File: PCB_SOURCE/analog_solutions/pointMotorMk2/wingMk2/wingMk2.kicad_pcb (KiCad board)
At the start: 2 copper layers, 46 x 23.3 mm, 0 parts

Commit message: added missing files. working on ossd mk2 code
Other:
- board size 46 x 23.3 mm -> 46 x 23.5 mm
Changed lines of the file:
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@@
 	)
 	(gr_arc
-		(start -18 -10.8)
-		(mid -17.707107 -11.507107)
-		(end -17 -11.8)
+		(start -18 -11)
+		(mid -17.707107 -11.707107)
+		(end -17 -12)
 		(stroke
 			(width 0.05)
@@
 	)
 	(gr_arc
-		(start -5 -9)
-		(mid -3.585786 -8.414214)
-		(end -3 -7)
+		(start 1.5 1.5)
+		(mid 0 3)
+		(end -1.5 1.5)
+		(stroke
+			(width 0.05)
+			(type default)
+		)
+		(layer "Edge.Cuts")
+	)
+	(gr_arc
+		(start -5.499999 -9)
+		(mid -4.085785 -8.414214)
+		(end -3.499999 -7)
 		(stroke
 			(width 0.05)
@@
 	)
 	(gr_line
-		(start 9 -7)
-		(end 9 1)
-		(stroke
-			(width 0.05)
-			(type default)
-		)
-		(layer "Edge.Cuts")
-	)
-	(gr_arc
-		(start 7 -9)
-		(mid 8.414214 -8.414214)
-		(end 9 -7)
-		(stroke
-			(width 0.05)
-			(type default)
-		)
-		(layer "Edge.Cuts")
-	)
-	(gr_line
-		(start -9 -7)
-		(end -9 1)
+		(start 9.500001 -7)
+		(end 9.500001 1)
+		(stroke
+			(width 0.05)
+			(type default)
+		)
+		(layer "Edge.Cuts")
+	)
+	(gr_arc
+		(start 7.500001 -9)
+		(mid 8.914215 -8.414214)
+		(end 9.500001 -7)
+		(stroke
+			(width 0.05)
+			(type default)
+		)
+		(layer "Edge.Cuts")
+	)
+	(gr_line
+		(start -9.499999 -7)
+		(end -9.499999 1)
 		(stroke
 			(width 0.05)
@@
 	)
 	(gr_arc
-		(start -9 -7)
-		(mid -8.414214 -8.414214)
-		(end -7 -9)
-		(stroke
-			(width 0.05)
-			(type default)
-		)
-		(layer "Edge.Cuts")
-	)
-	(gr_arc
-		(start 5.000001 2.999999)
-		(mid 3.585787 2.414213)
-		(end 3.000001 0.999999)
+		(start -9.499999 -7)
+		(mid -8.914213 -8.414214)
+		(end -7.499999 -9)
+		(stroke
+			(width 0.05)
+			(type default)
+		)
+		(layer "Edge.Cuts")
+	)
+	(gr_arc
+		(start 5.500002 2.999999)
+		(mid 4.085788 2.414213)
+		(end 3.500002 0.999999)
 		(stroke
 			(width 0.05)
@@
 	)
 	(gr_arc
-		(start 8.999999 0.999999)
-		(mid 8.414213 2.414213)
-		(end 6.999999 2.999999)
-		(stroke
-			(width 0.05)
-			(type default)
-		)
-		(layer "Edge.Cuts")
-	)
-	(gr_arc
-		(start -6.999999 2.999999)
-		(mid -8.414213 2.414213)
-		(end -8.999999 0.999999)
+		(start 9.5 0.999999)
+		(mid 8.914214 2.414213)
+		(end 7.5 2.999999)
+		(stroke
+			(width 0.05)
+			(type default)
+		)
+		(layer "Edge.Cuts")
+	)
+	(gr_arc
+		(start -7.499998 2.999999)
+		(mid -8.914212 2.414213)
+		(end -9.499998 0.999999)
 		(stroke
 			(width 0.05)
@@
 	)
 	(gr_line
-		(start 5.000001 2.999999)
-		(end 6.999999 2.999999)
+		(start 5.500002 2.999999)
+		(end 7.5 2.999999)
+		(stroke
+			(width 0.05)
+			(type default)
+		)
+		(layer "Edge.Cuts")
+	)
+	(gr_arc
+		(start -1.5 -7.5)
+		(mid 0 -9)
+		(end 1.5 -7.5)
 		(stroke
 			(width 0.05)
@@
 	)
 	(gr_line
-		(start -1 -7)
-		(end -1 1)
+		(start -1.5 -7.5)
+		(end -1.5 1.5)
 		(stroke
 			(width 0.05)
@@
 	)
 	(gr_line
-		(start -3 -7)
-		(end -3 1)
-		(stroke
-			(width 0.05)
-			(type default)
-		)
-		(layer "Edge.Cuts")
-	)
-	(gr_line
-		(start 28 -6.75)
+		(start -3.499999 -7)
+		(end -3.499999 1)
+		(stroke
+			(width 0.05)
+			(type default)
+		)
+		(layer "Edge.Cuts")
+	)
+	(gr_line
+		(start 28 -6.95)
 		(end 28 3.5)
 		(stroke
@@
 		(layer "Edge.Cuts")
 	)
-	(gr_arc
-		(start 1 1)
-		(mid 0 2)
-		(end -1 1)
-		(stroke
-			(width 0.05)
-			(type default)
-		)
-		(layer "Edge.Cuts")
-	)
-	(gr_line
-		(start 5 -9)
-		(end 7 -9)
-		(stroke
-			(width 0.05)
-			(type default)
-		)
-		(layer "Edge.Cuts")
-	)
-	(gr_arc
-		(start -1 -7)
-		(mid 0 -8)
-		(end 1 -7)
-		(stroke
-			(width 0.05)
-			(type default)
-		)
-		(layer "Edge.Cuts")
-	)
-	(gr_arc
-		(start -3.000001 0.999999)
-		(mid -3.585787 2.414213)
-		(end -5.000001 2.999999)
+	(gr_line
+		(start 5.500001 -9)
+		(end 7.500001 -9)
+		(stroke
+			(width 0.05)
+			(type default)
+		)
+		(layer "Edge.Cuts")
+	)
+	(gr_arc
+		(start -3.5 0.999999)
+		(mid -4.085786 2.414213)
+		(end -5.5 2.999999)
 		(stroke
 			(width 0.05)
@@
 	)
 	(gr_line
-		(start 3 -7)
-		(end 3 1)
-		(stroke
-			(width 0.05)
-			(type default)
-		)
-		(layer "Edge.Cuts")
-	)
-	(gr_line
-		(start 4 -13.3)
-		(end 4 -11.8)
+		(start 3.500001 -7)
+		(end 3.500001 1)
+		(stroke
+			(width 0.05)
+			(type default)
+		)
+		(layer "Edge.Cuts")
+	)
+	(gr_line
+		(start 4 -13.5)
+		(end 4 -12)
 		(stroke
 			(width 0.05)
@@
 	)
 	(gr_line
-		(start -17 -11.8)
-		(end -4 -11.8)
-		(stroke
-			(width 0.05)
-			(type default)
-		)
-		(layer "Edge.Cuts")
-	)
-	(gr_line
-		(start -4 -13.3)
-		(end 4 -13.3)
-		(stroke
-			(width 0.05)
-			(type default)
-		)
-		(layer "Edge.Cuts")
-	)
-	(gr_line
-		(start -7 -9)
-		(end -5 -9)
-		(stroke
-			(width 0.05)
-			(type default)
-		)
-		(layer "Edge.Cuts")
-	)
-	(gr_arc
-		(start 3 -7)
-		(mid 3.585786 -8.414214)
-		(end 5 -9)
-		(stroke
-			(width 0.05)
-			(type default)
-		)
-		(layer "Edge.Cuts")
-	)
-	(gr_line
-		(start 4 -11.8)
-		(end 23 -11.8)
+		(start -17 -12)
+		(end -4 -12)
+		(stroke
+			(width 0.05)
+			(type default)
+		)
+		(layer "Edge.Cuts")
+	)
+	(gr_line
+		(start -4 -13.5)
+		(end 4 -13.5)
+		(stroke
+			(width 0.05)
+			(type default)
+		)
+		(layer "Edge.Cuts")
+	)
+	(gr_line
+		(start -7.499999 -9)
+		(end -5.499999 -9)
+		(stroke
+			(width 0.05)
+			(type default)
+		)
+		(layer "Edge.Cuts")
+	)
+	(gr_arc
+		(start 3.500001 -7)
+		(mid 4.085787 -8.414214)
+		(end 5.500001 -9)
+		(stroke
+			(width 0.05)
+			(type default)
+		)
+		(layer "Edge.Cuts")
+	)
+	(gr_line
+		(start 4 -12)
+		(end 23 -12)
 		(stroke
 			(width 0.05)
@@
 	(gr_line
 		(start -18 7.5)
-		(end -18 -10.8)
+		(end -18 -11)
 		(stroke
 			(width 0.05)
@@
 	)
 	(gr_line
-		(start 1 1)
-		(end 1 -7)
-		(stroke
-			(width 0.05)
-			(type default)
-		)
-		(layer "Edge.Cuts")
-	)
-	(gr_line
-		(start -6.999999 2.999999)
-		(end -5.000001 2.999999)
-		(stroke
-			(width 0.05)
-			(type default)
-		)
-		(layer "Edge.Cuts")
-	)
-	(gr_arc
-		(start 23 -11.8)
-		(mid 26.545889 -10.310534)
-		(end 28 -6.75)
+		(start 1.5 1.5)
+		(end 1.5 -7.5)
+		(stroke
+			(width 0.05)
+			(type default)
+		)
+		(layer "Edge.Cuts")
+	)
+	(gr_line
+		(start -7.499998 2.999999)
+		(end -5.5 2.999999)
+		(stroke
+			(width 0.05)
+			(type default)
+		)
+		(layer "Edge.Cuts")
+	)
+	(gr_arc
+		(start 23 -12)
+		(mid 26.545889 -10.510534)
+		(end 28 -6.95)
 		(stroke
 			(width 0.05)
@@
 	)
 	(gr_line
-		(start -4 -11.8)
-		(end -4 -13.3)
-		(stroke
-			(width 0.05)
+		(start -4 -12)
+		(end -4 -13.5)
+		(stroke
+			(width 0.05)

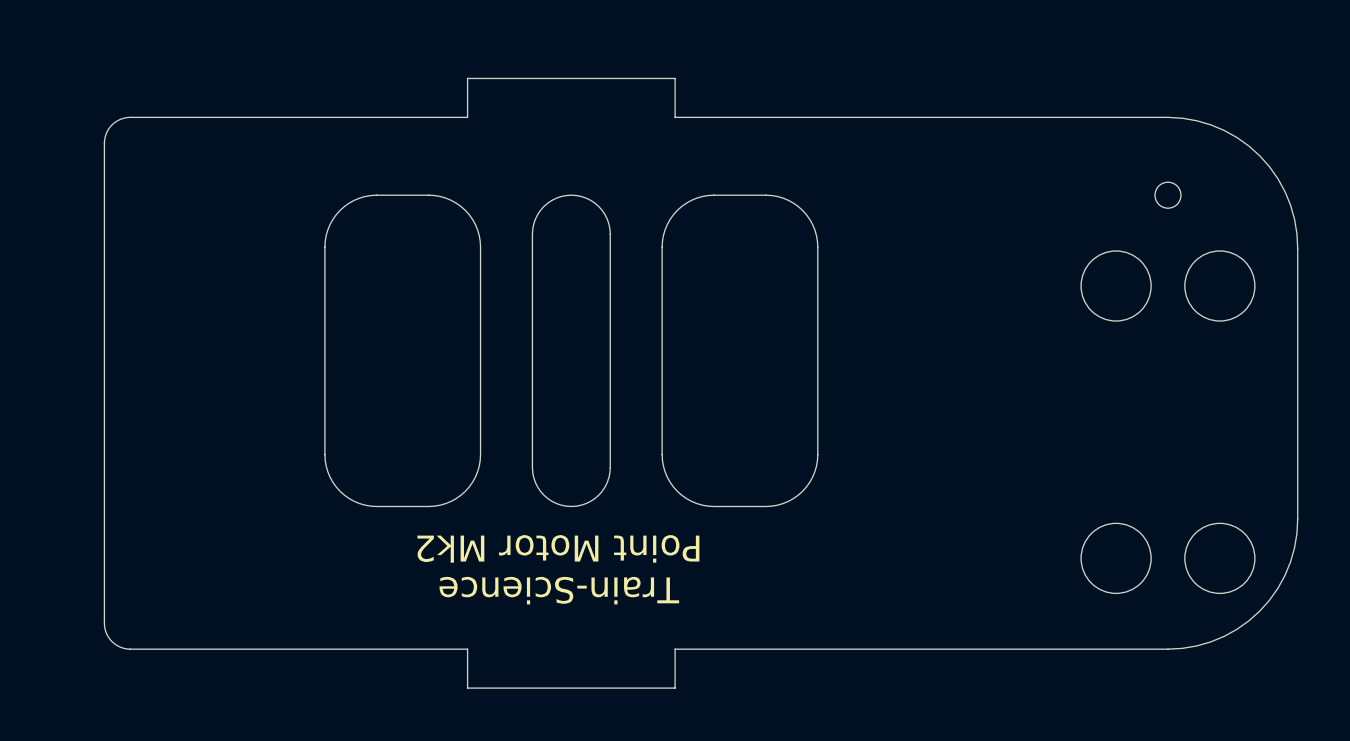
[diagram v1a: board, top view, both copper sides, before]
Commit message: fixed bug in ahob program among others
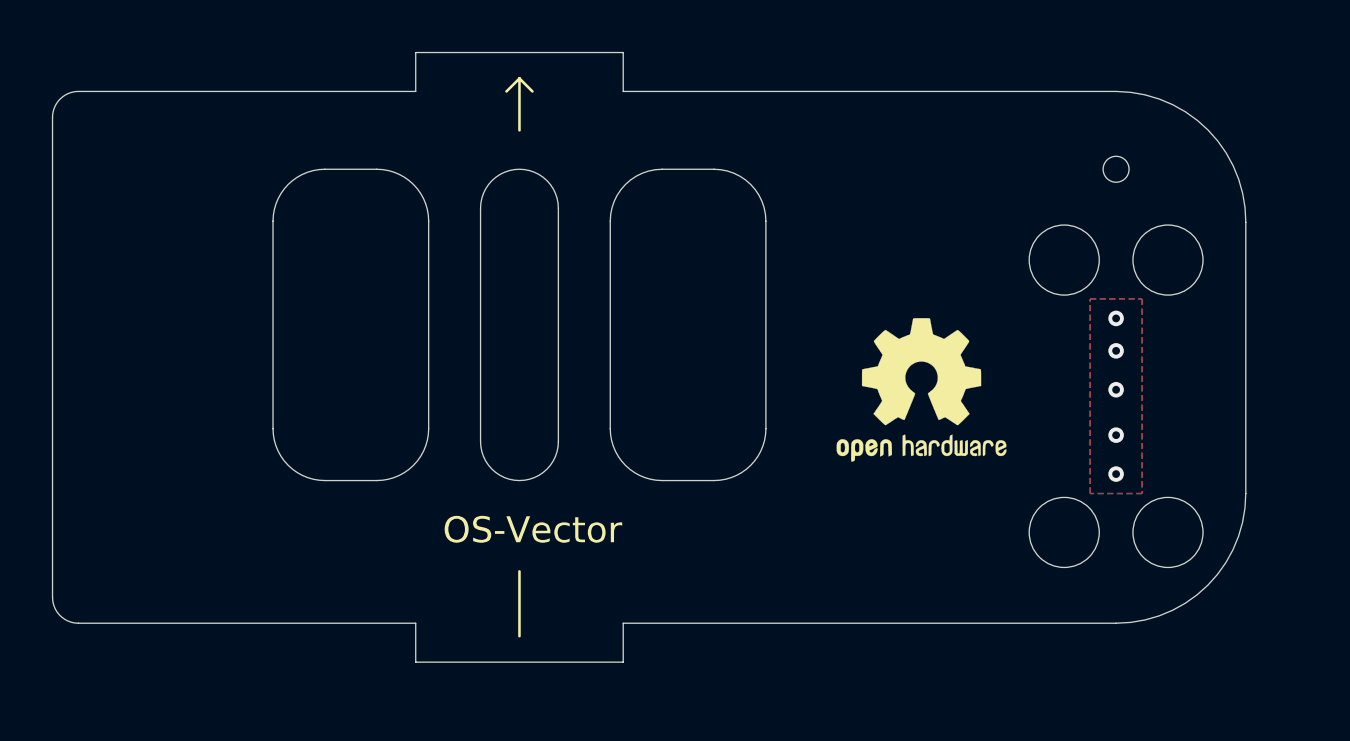
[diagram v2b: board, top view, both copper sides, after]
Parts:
- added REF**: OSHW-Logo2_7.3x6mm_SilkScreen, Symbol:OSHW-Logo2_7.3x6mm_SilkScreen, F.Cu at (13.5, -1.50)
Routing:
- net GND: vias 0 -> 5
- added copper zone on B.Cu, net GND
- added copper zone on F.Cu, net GND
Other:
- board text added: "OS-Vector"
- board text removed: "Train-Science Point Motor Mk2"
